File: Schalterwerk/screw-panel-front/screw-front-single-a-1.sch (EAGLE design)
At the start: 15 parts, among them J1 M4-SCREW-HOLE, J2 M4-SCREW-HOLE, J3 M4-SCREW-HOLE, J4 M4-SCREW-HOLE, J5 M4-SCREW-HOLE, J6 M4-SCREW-HOLE, J7 M4-SCREW-HOLE, J8 M4-SCREW-HOLE, X1 PHNX_4P_350CONN_1984989_PXC, X2 PHNX_4P_350CONN_1984989_PXC

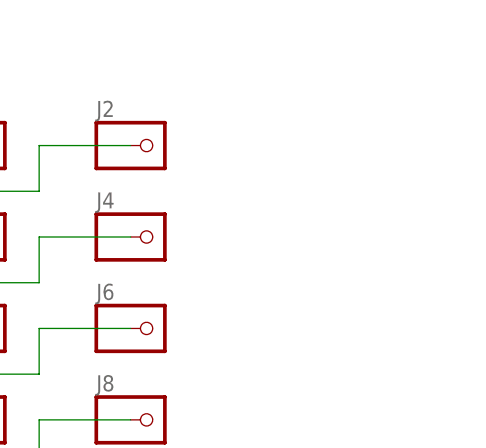
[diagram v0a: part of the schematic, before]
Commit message: Adds alignment holes.
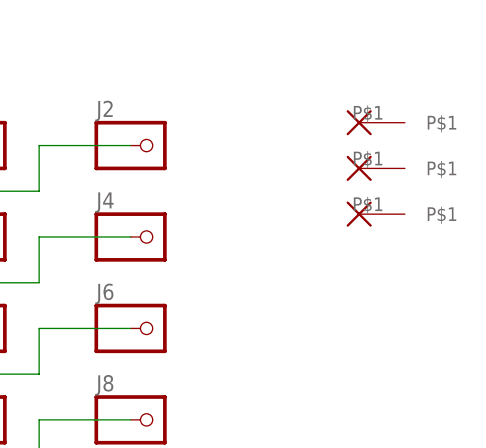
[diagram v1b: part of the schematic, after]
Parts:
- added H5, H6, H7: ALIGN-HOLE, eagleparts:ALIGN-HOLE
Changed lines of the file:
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@@
 <layer number="113" name="ReferenceLS" color="7" fill="1" visible="no" active="no"/>
 <layer number="114" name="programming" color="7" fill="1" visible="yes" active="yes"/>
+<layer number="115" name="laser-etch" color="47" fill="1" visible="no" active="yes"/>
 <layer number="116" name="Patch_BOT" color="9" fill="4" visible="no" active="yes"/>
+<layer number="117" name="laser-cut" color="63" fill="1" visible="yes" active="yes"/>
 <layer number="118" name="Rect_Pads" color="7" fill="1" visible="no" active="no"/>
 <layer number="121" name="_tsilk" color="7" fill="1" visible="no" active="yes"/>
@@
 <part name="JP4" library="pinhead" library_urn="urn:adsk.eagle:library:325" deviceset="PINHD-1X3" device="" package3d_urn="urn:adsk.eagle:package:22458/2"/>
 <part name="SJ1" library="eagleparts" deviceset="SJ" device="RND2"/>
+<part name="H5" library="eagleparts" deviceset="ALIGN-HOLE" device=""/>
+<part name="H6" library="eagleparts" deviceset="ALIGN-HOLE" device=""/>
+<part name="H7" library="eagleparts" deviceset="ALIGN-HOLE" device=""/>
 </parts>
 <sheets>
@@
 <attribute name="VALUE" x="24.13" y="120.904" size="1.778" layer="96" rot="R90"/>
 </instance>
+<instance part="H5" gate="G$1" x="134.62" y="142.24" smashed="yes"/>
+<instance part="H6" gate="G$1" x="134.62" y="137.16" smashed="yes"/>
+<instance part="H7" gate="G$1" x="134.62" y="132.08" smashed="yes"/>
 </instances>
 <busses>
